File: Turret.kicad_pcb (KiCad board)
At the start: 2 copper layers, 10 parts, among them J12 Conn_01x02_Pin, J13 Conn_01x02_Pin, J2 Conn_01x02_Pin, J3 Conn_01x02_Pin, J4 Conn_01x02_Pin, J5 Conn_01x02_Pin, J6 Conn_01x02_Pin, J7 Conn_01x02_Pin, J8 Conn_01x02_Pin, J9 Conn_01x02_Pin

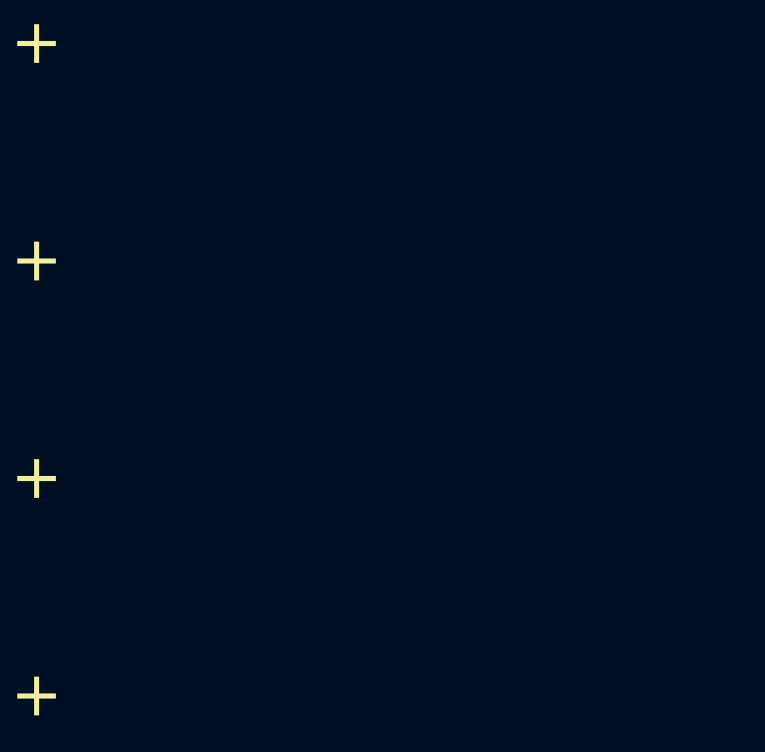
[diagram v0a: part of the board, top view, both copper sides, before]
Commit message: Added footprint for aviator
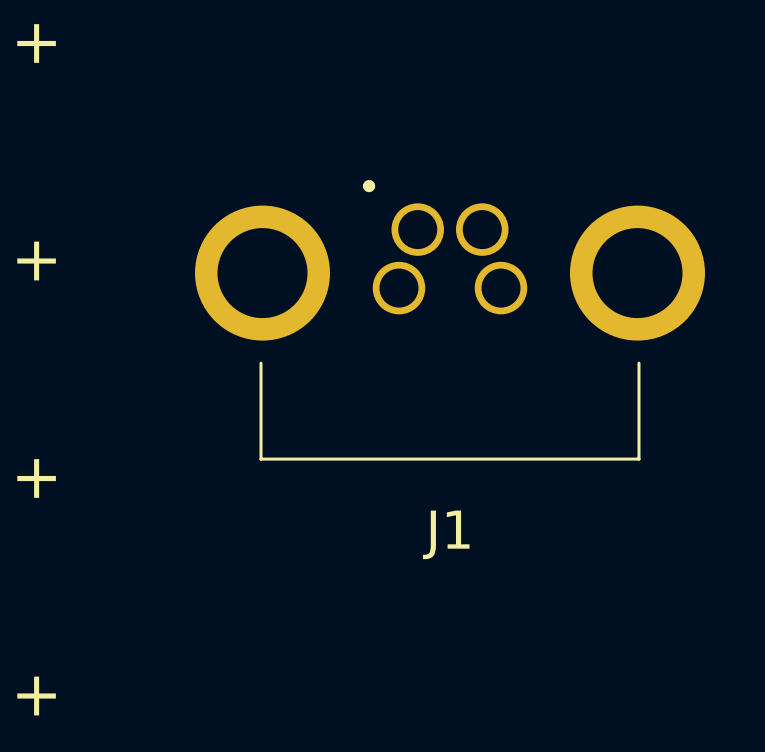
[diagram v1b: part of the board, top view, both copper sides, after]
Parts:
- added J1: Conn_01x04_Pin, Robomasters:866319112100004, F.Cu at (94.8, 73.2)
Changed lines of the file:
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@@
   (net 3 "Net-(J3-Pin_1)")
   (net 4 "Net-(J3-Pin_2)")
-  (net 5 "Net-(Feeder1-VIN)")
-  (net 6 "Net-(Feeder1-GND)")
-  (net 7 "Net-(Feeder1-CANH)")
-  (net 8 "Net-(Feeder1-CANL)")
+  (net 5 "Net-(J1-Pin_1)")
+  (net 6 "Net-(J1-Pin_2)")
+  (net 7 "Net-(J1-Pin_3)")
+  (net 8 "Net-(J1-Pin_4)")
   (net 9 "Net-(J6-Pin_1)")
   (net 10 "Net-(J6-Pin_2)")
@@
   (net 19 "Net-(J13-Pin_1)")
   (net 20 "Net-(J13-Pin_2)")
+  (net 21 "Net-(J4-Pin_1)")
+  (net 22 "Net-(J4-Pin_2)")
+  (net 23 "Net-(J5-Pin_1)")
+  (net 24 "Net-(J5-Pin_2)")
   (footprint "Connector_JST:JST_GH_BM02B-GHS-TBT_1x02-1MP_P1.25mm_Vertical" (layer "F.Cu")
     (at 66.11 72.83)
@@
       (stroke (width 0.1) (type solid)) (layer "F.Fab"))
     (pad "1" smd roundrect (at -0.625 1.95) (size 0.6 1.7) (layers "F.Cu" "F.Paste" "F.Mask") (roundrect_rratio 0.25)
-      (net 7 "Net-(Feeder1-CANH)") (pinfunction "Pin_1") (pintype "passive"))
+      (net 23 "Net-(J5-Pin_1)") (pinfunction "Pin_1") (pintype "passive"))
     (pad "2" smd roundrect (at 0.625 1.95) (size 0.6 1.7) (layers "F.Cu" "F.Paste" "F.Mask") (roundrect_rratio 0.25)
-      (net 8 "Net-(Feeder1-CANL)") (pinfunction "Pin_2") (pintype "passive"))
+      (net 24 "Net-(J5-Pin_2)") (pinfunction "Pin_2") (pintype "passive"))
     (pad "MP" smd roundrect (at -2.475 -1.4) (size 1 2.8) (layers "F.Cu" "F.Paste" "F.Mask") (roundrect_rratio 0.25))
     (pad "MP" smd roundrect (at 2.475 -1.4) (size 1 2.8) (layers "F.Cu" "F.Paste" "F.Mask") (roundrect_rratio 0.25))
@@
       (stroke (width 0.1) (type solid)) (layer "F.Fab"))
     (pad "1" thru_hole rect (at 0 0) (size 3.8 3.8) (drill 2.7) (layers "*.Cu" "*.Mask")
-      (net 5 "Net-(Feeder1-VIN)") (pinfunction "Pin_1") (pintype "passive"))
+      (net 21 "Net-(J4-Pin_1)") (pinfunction "Pin_1") (pintype "passive"))
     (pad "2" thru_hole circle (at 5 0) (size 4 4) (drill 2.7) (layers "*.Cu" "*.Mask")
-      (net 6 "Net-(Feeder1-GND)") (pinfunction "Pin_2") (pintype "passive"))
+      (net 22 "Net-(J4-Pin_2)") (pinfunction "Pin_2") (pintype "passive"))
     (model "${KICAD6_3DMODEL_DIR}/Connector_AMASS.3dshapes/AMASS_XT30U-F_1x02_P5.0mm_Vertical.wrl"
       (offset (xyz 0 0 0))
@@
     )
   )
+  (footprint "Robomasters:866319112100004" (layer "F.Cu")
+    (at 94.82 73.1815)
+    (descr "86 6319 1121 00004-1")
+    (tags "Connector")
+    (property "Sheetfile" "Turret.kicad_sch")
+    (property "Sheetname" "")
+    (property "ki_description" "Generic connector, single row, 01x04, script generated")
+    (property "ki_keywords" "connector")
+    (attr through_hole)
+    (fp_text reference "J1" (at 1.7 8.099) (layer "F.SilkS")
+        (effects (font (size 1.27 1.27) (thickness 0.254)))
+    )
+    (fp_text value "Conn_01x04_Pin" (at 1.7 8.099) (layer "F.SilkS") hide
+        (effects (font (size 1.27 1.27) (thickness 0.254)))
+    )
+    (fp_text user "${REFERENCE}" (at 1.7 8.099) (layer "F.Fab")
+        (effects (font (size 1.27 1.27) (thickness 0.254)))
+    )
+    (fp_line (start -4.6 2.5) (end -4.6 5.7)
+      (stroke (width 0.1) (type solid)) (layer "F.SilkS"))
+    (fp_line (start -4.6 5.7) (end 8 5.7)
+      (stroke (width 0.1) (type solid)) (layer "F.SilkS"))
+    (fp_line (start -1.1 -3.4) (end -1.1 -3.4)
+      (stroke (width 0.2) (type solid)) (layer "F.SilkS"))
+    (fp_line (start -0.894 -3.4) (end -0.894 -3.4)
+      (stroke (width 0.2) (type solid)) (layer "F.SilkS"))
+    (fp_line (start 8 5.7) (end 8 2.5)
+      (stroke (width 0.1) (type solid)) (layer "F.SilkS"))
+    (fp_arc (start -1.1 -3.4) (mid -0.997 -3.503) (end -0.894 -3.4)
+      (stroke (width 0.2) (type solid)) (layer "F.SilkS"))
+    (fp_arc (start -0.894 -3.4) (mid -0.997 -3.297) (end -1.1 -3.4)
+      (stroke (width 0.2) (type solid)) (layer "F.SilkS"))
+    (fp_line (start -7.8 -4.503) (end 11.2 -4.503)
+      (stroke (width 0.1) (type solid)) (layer "F.CrtYd"))
+    (fp_line (start -7.8 20.7) (end -7.8 -4.503)
+      (stroke (width 0.1) (type solid)) (layer "F.CrtYd"))
+    (fp_line (start 11.2 -4.503) (end 11.2 20.7)
+      (stroke (width 0.1) (type solid)) (layer "F.CrtYd"))
+    (fp_line (start 11.2 20.7) (end -7.8 20.7)
+      (stroke (width 0.1) (type solid)) (layer "F.CrtYd"))
+    (fp_line (start -4.6 -2.8) (end 8 -2.8)
+      (stroke (width 0.2) (type solid)) (layer "F.Fab"))
+    (fp_line (start -4.6 5.7) (end -4.6 -2.8)
+      (stroke (width 0.2) (type solid)) (layer "F.Fab"))
+    (fp_line (start -3.3 5.7) (end -3.3 8.5)
+      (stroke (width 0.2) (type solid)) (layer "F.Fab"))
+    (fp_line (start -3.3 8.5) (end 6.7 8.5)
+      (stroke (width 0.2) (type solid)) (layer "F.Fab"))
+    (fp_line (start -2.6 8.5) (end -2.6 17.5)
+      (stroke (width 0.2) (type solid)) (layer "F.Fab"))
+    (fp_line (start -2.6 17.5) (end 6 17.5)
+      (stroke (width 0.2) (type solid)) (layer "F.Fab"))
+    (fp_line (start -1.8 17.5) (end -1.8 19.7)
+      (stroke (width 0.2) (type solid)) (layer "F.Fab"))
+    (fp_line (start -1.8 19.7) (end 5.2 19.7)
+      (stroke (width 0.2) (type solid)) (layer "F.Fab"))
+    (fp_line (start 5.2 19.7) (end 5.2 17.5)
+      (stroke (width 0.2) (type solid)) (layer "F.Fab"))
+    (fp_line (start 6 17.5) (end 6 8.5)
+      (stroke (width 0.2) (type solid)) (layer "F.Fab"))
+    (fp_line (start 6.7 8.5) (end 6.7 5.7)
+      (stroke (width 0.2) (type solid)) (layer "F.Fab"))
+    (fp_line (start 8 -2.8) (end 8 5.7)
+      (stroke (width 0.2) (type solid)) (layer "F.Fab"))
+    (fp_line (start 8 5.7) (end -4.6 5.7)
+      (stroke (width 0.2) (type solid)) (layer "F.Fab"))
+    (pad "1" thru_hole circle (at 0 0) (size 1.75 1.75) (drill 1.3) (layers "*.Cu" "*.Mask")
+      (net 5 "Net-(J1-Pin_1)") (pinfunction "Pin_1") (pintype "passive"))
+    (pad "2" thru_hole circle (at 0.625 -1.95) (size 1.75 1.75) (drill 1.3) (layers "*.Cu" "*.Mask")
+      (net 6 "Net-(J1-Pin_2)") (pinfunction "Pin_2") (pintype "passive"))
+    (pad "3" thru_hole circle (at 3.4 0) (size 1.75 1.75) (drill 1.3) (layers "*.Cu" "*.Mask")
+      (net 7 "Net-(J1-Pin_3)") (pinfunction "Pin_3") (pintype "passive"))
+    (pad "4" thru_hole circle (at 2.775 -1.95) (size 1.75 1.75) (drill 1.3) (layers "*.Cu" "*.Mask")
+      (net 8 "Net-(J1-Pin_4)") (pinfunction "Pin_4") (pintype "passive"))
+    (pad "MH1" thru_hole circle (at -4.55 -0.5) (size 4.5 4.5) (drill 3) (layers "*.Cu" "*.Mask"))
+    (pad "MH2" thru_hole circle (at 7.95 -0.5) (size 4.5 4.5) (drill 3) (layers "*.Cu" "*.Mask"))
+  )
   (footprint "Connector_JST:JST_GH_BM02B-GHS-TBT_1x02-1MP_P1.25mm_Vertical" (layer "F.Cu")

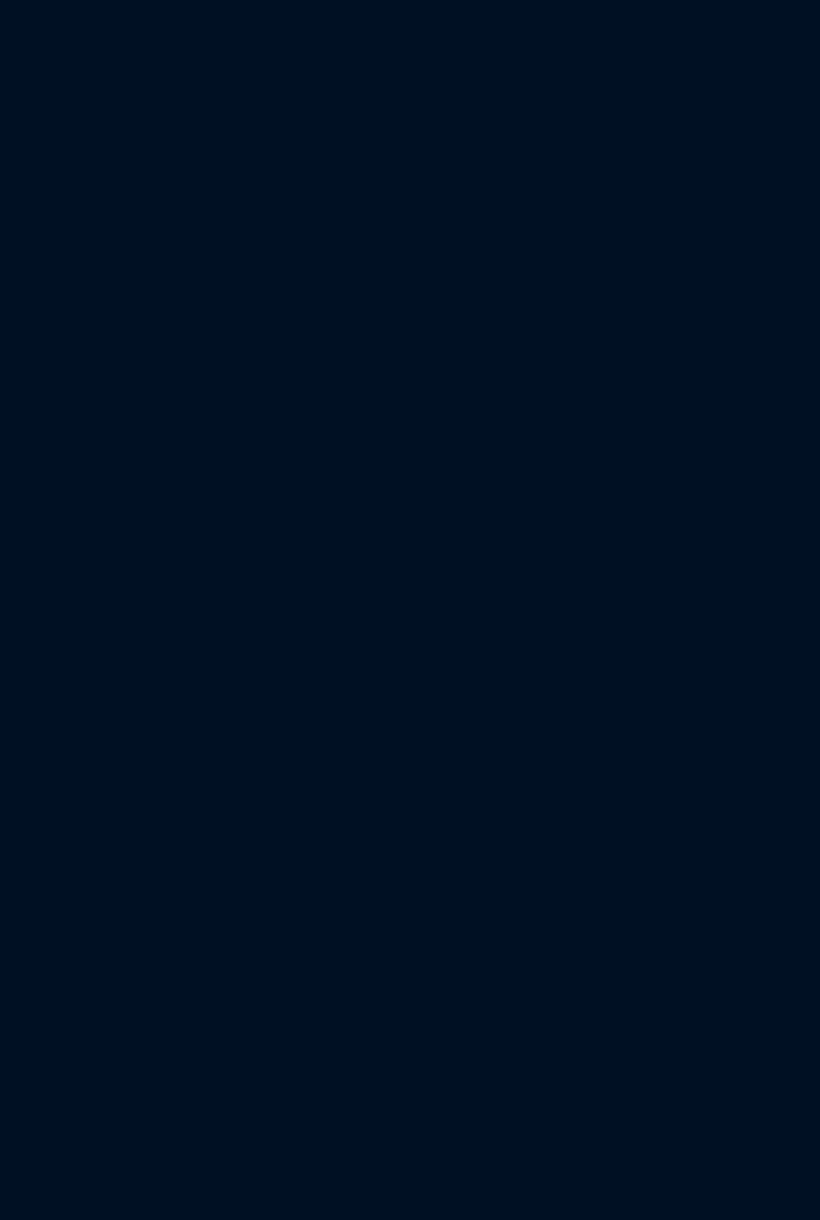
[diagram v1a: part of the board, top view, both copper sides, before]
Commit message: Update turret
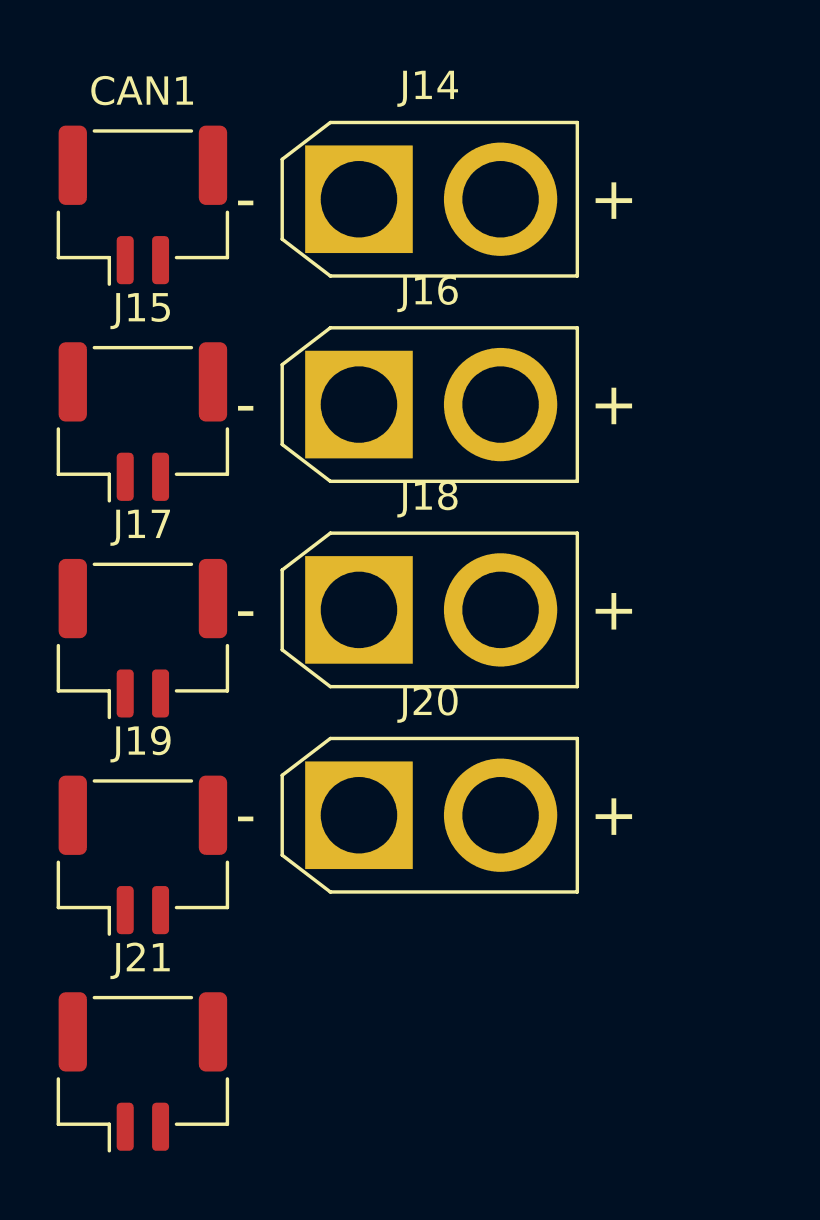
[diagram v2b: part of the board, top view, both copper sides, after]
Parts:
- added CAN1: Conn_01x02_Pin, Connector_JST:JST_GH_BM02B-GHS-TBT_1x02-1MP_P1.25mm_Vertical, F.Cu at (33.1, 64.8)
- added J14: Conn_01x02_Pin, Connector_AMASS:AMASS_XT30U-F_1x02_P5.0mm_Vertical, F.Cu at (40.7, 64.6)
- added J15: Conn_01x02_Pin, Connector_JST:JST_GH_BM02B-GHS-TBT_1x02-1MP_P1.25mm_Vertical, F.Cu at (33.1, 72.5)
- added J16: Conn_01x02_Pin, Connector_AMASS:AMASS_XT30U-F_1x02_P5.0mm_Vertical, F.Cu at (40.7, 71.9)
- added J17: Conn_01x02_Pin, Connector_JST:JST_GH_BM02B-GHS-TBT_1x02-1MP_P1.25mm_Vertical, F.Cu at (33.1, 80.1)
- added J18: Conn_01x02_Pin, Connector_AMASS:AMASS_XT30U-F_1x02_P5.0mm_Vertical, F.Cu at (40.7, 79.1)
- added J19: Conn_01x02_Pin, Connector_JST:JST_GH_BM02B-GHS-TBT_1x02-1MP_P1.25mm_Vertical, F.Cu at (33.1, 87.8)
- added J20: Conn_01x02_Pin, Connector_AMASS:AMASS_XT30U-F_1x02_P5.0mm_Vertical, F.Cu at (40.7, 86.4)
- added J21: Conn_01x02_Pin, Connector_JST:JST_GH_BM02B-GHS-TBT_1x02-1MP_P1.25mm_Vertical, F.Cu at (33.1, 95.4)
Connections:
- J2 pad 1: Net-(J2-Pin_1) -> GND1
- J2 pad 2: Net-(J2-Pin_2) -> /Turret_Vin
- J3 pad 1: Net-(J3-Pin_1) -> /Turret_CANL
- J3 pad 2: Net-(J3-Pin_2) -> /Turret_CANH

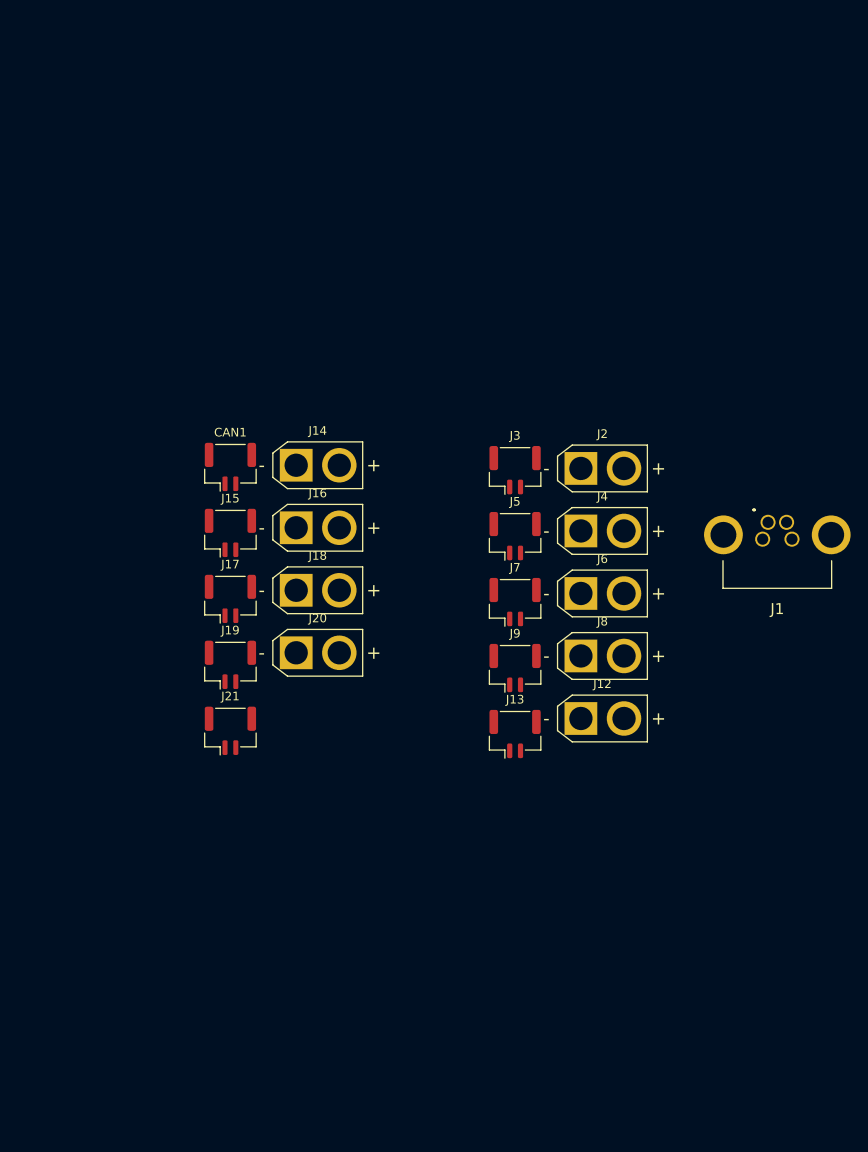
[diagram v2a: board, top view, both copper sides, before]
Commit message: Updated PCB to use unified power 6 pin, added 2 1x2 connectors
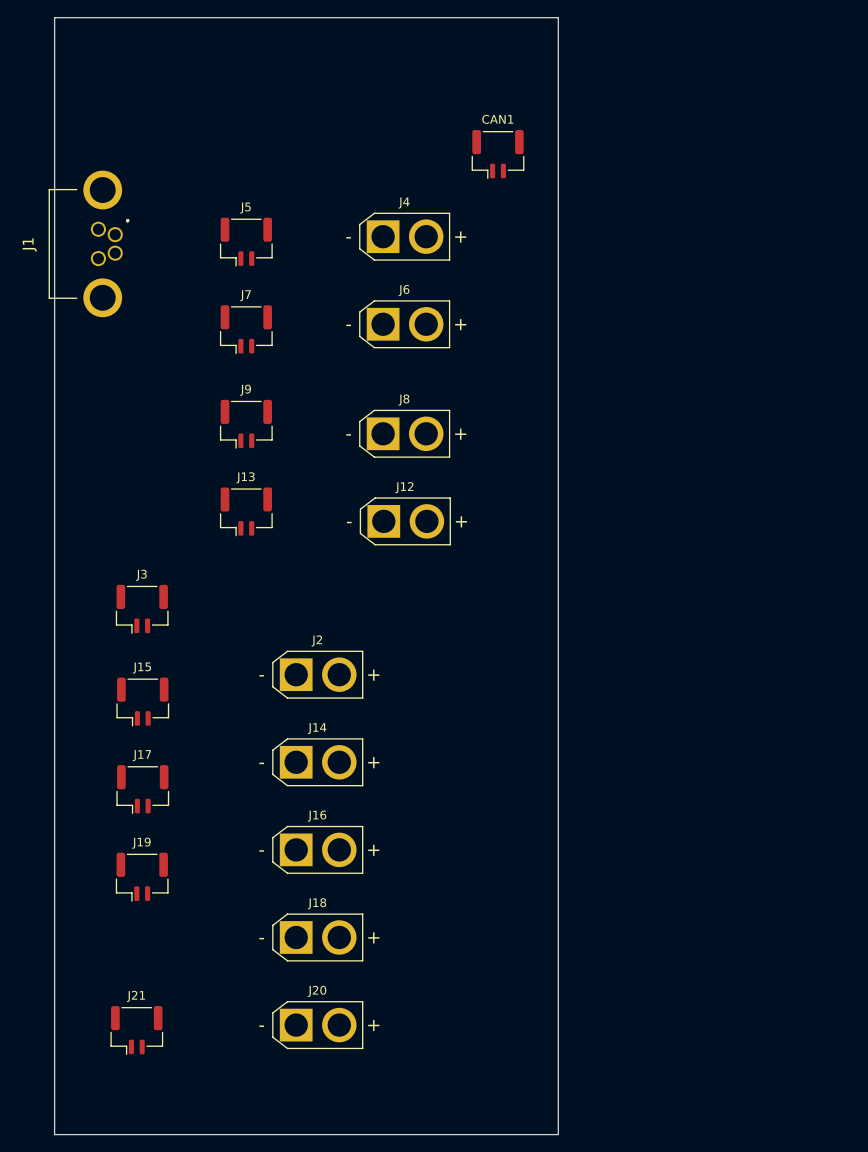
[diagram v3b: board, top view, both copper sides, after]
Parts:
- moved J1 85.0 mm to (17.8, 37.2), turned to -90 degrees
- moved CAN1 47.7 mm to (64.1, 28.5)
- moved J5 46.2 mm to (34.9, 38.7)
- moved J3 46.1 mm to (22.9, 81.3)
- moved J7 44.4 mm to (34.9, 48.9)
- moved J20 43.2 mm to (40.7, 129.5)
- moved J9 42.1 mm to (34.9, 59.8)
- moved J4 41.1 mm to (50.8, 38.1)
- moved J2 40.8 mm to (40.7, 88.9)
- moved J13 40.5 mm to (34.9, 70.0)
- moved J18 40.3 mm to (40.7, 119.4)
- moved J6 38.7 mm to (50.8, 48.3)
- moved J16 37.4 mm to (40.7, 109.2)
- moved J21 36.4 mm to (22.2, 130.1)
- moved J8 34.5 mm to (50.8, 61.0)
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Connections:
- J14 pad 2: /Turret_Vin -> /Shooter_Vin
- J15 pad 1: /Turret_CANL -> /Shooter_CANL
- J15 pad 2: /Turret_CANH -> /Shooter_CANH
- J16 pad 2: /Turret_Vin -> /Shooter_Vin
- J17 pad 1: /Turret_CANL -> /Shooter_CANL
- J17 pad 2: /Turret_CANH -> /Shooter_CANH
- J18 pad 2: /Turret_Vin -> /Shooter_Vin
- J19 pad 1: /Turret_CANL -> /Shooter_CANL
- J19 pad 2: /Turret_CANH -> /Shooter_CANH
- J2 pad 2: /Turret_Vin -> /Shooter_Vin
- J20 pad 2: /Chassis_Vin -> /Turret_Vin
- J21 pad 1: /Chassis_CANL -> /Turret_CANL
- J21 pad 2: /Chassis_CANH -> /Turret_CANH
- J3 pad 1: /Turret_CANL -> /Shooter_CANL
- J3 pad 2: /Turret_CANH -> /Shooter_CANH
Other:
- board outline added: 58.4 x 129.5 mm
